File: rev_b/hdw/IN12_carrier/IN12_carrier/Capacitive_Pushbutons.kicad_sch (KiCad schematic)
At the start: 31 parts, among them J1001 Cap SNS

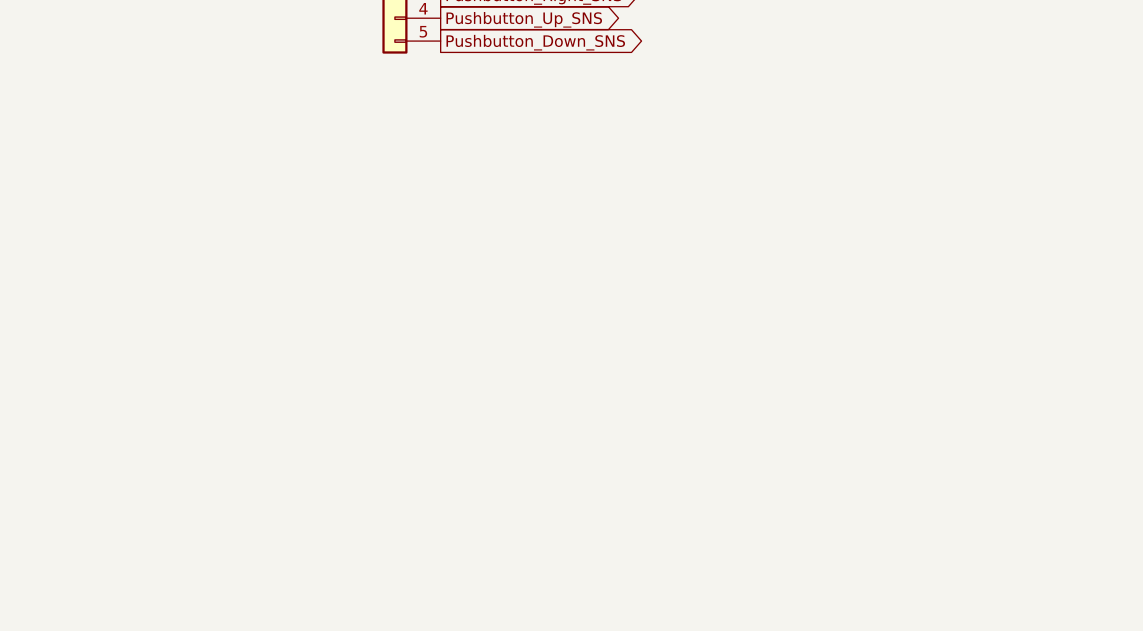
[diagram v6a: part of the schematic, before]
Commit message: added BOM for IN12 carrier, finished routing, some schematic tweaks, adjusted design rules for ERC
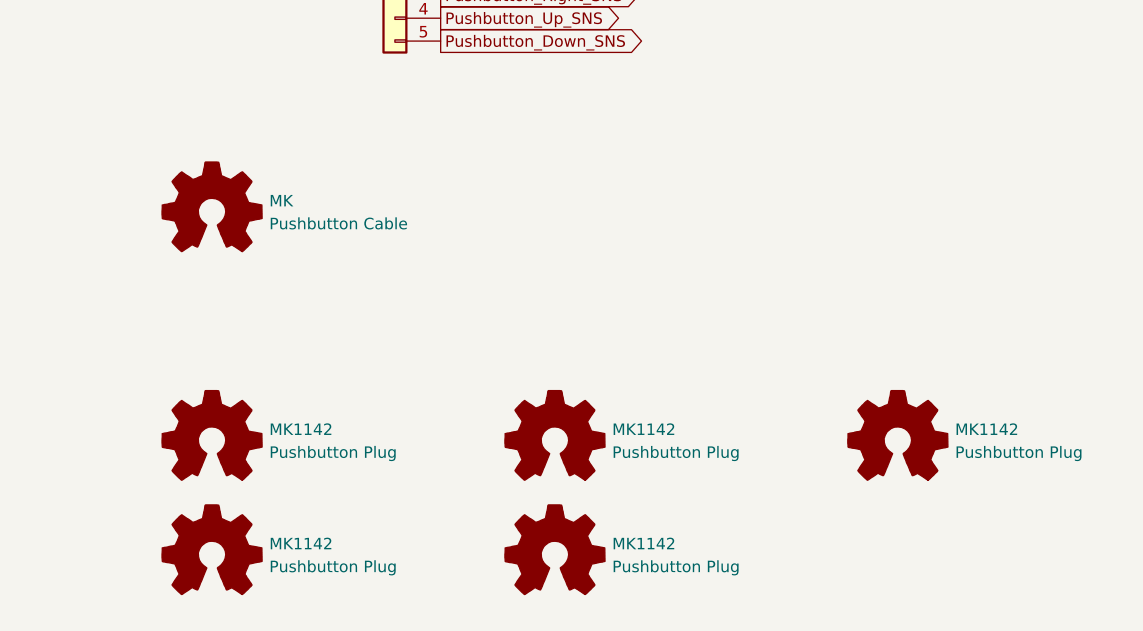
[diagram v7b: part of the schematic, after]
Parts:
- added MK: Pushbutton Cable, symbol Graphic:Logo_Open_Hardware_Small
- added MK1142 (x5): Pushbutton Plug, symbol Graphic:Logo_Open_Hardware_Small
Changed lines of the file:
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@@
+    )
+  )
+  (symbol (lib_id "Graphic:Logo_Open_Hardware_Small") (at 238.76 147.32 0) (unit 1)
+    (in_bom no) (on_board no) (dnp no) (fields_autoplaced)
+    (property "Reference" "MK1142" (at 245.11 146.05 0)
+      (effects (font (size 1.27 1.27)) (justify left))
+    )
+    (property "Value" "Pushbutton Plug" (at 245.11 148.59 0)
+      (effects (font (size 1.27 1.27)) (justify left))
+    )
+    (property "Footprint" "" (at 238.76 147.32 0)
+      (effects (font (size 1.27 1.27)) hide)
+    )
+    (property "Datasheet" "~" (at 238.76 147.32 0)
+      (effects (font (size 1.27 1.27)) hide)
+    )
+    (property "Digi-Key PN" "36-7600-ND" (at 238.76 147.32 0)
+      (effects (font (size 1.27 1.27)) hide)
+    )
+    (instances
+      (project "IN12_carrier"
+        (path "/c4d83a5b-e6ae-4326-9df5-0c4ac01f7d8c/3ccac04c-3fb1-4fbb-89c4-5dc2f5c153e1"
+          (reference "MK1142") (unit 1)
+        )
+        (path "/c4d83a5b-e6ae-4326-9df5-0c4ac01f7d8c/1c22c65e-aaf7-48af-ba9d-ccdda03c7a98"
+          (reference "MK1006") (unit 1)
+        )
+      )
     )
   )
@@
     )
   )
+  (symbol (lib_id "Graphic:Logo_Open_Hardware_Small") (at 162.56 160.02 0) (unit 1)
+    (in_bom no) (on_board no) (dnp no) (fields_autoplaced)
+    (property "Reference" "MK1142" (at 168.91 158.75 0)
+      (effects (font (size 1.27 1.27)) (justify left))
+    )
+    (property "Value" "Pushbutton Plug" (at 168.91 161.29 0)
+      (effects (font (size 1.27 1.27)) (justify left))
+    )
+    (property "Footprint" "" (at 162.56 160.02 0)
+      (effects (font (size 1.27 1.27)) hide)
+    )
+    (property "Datasheet" "~" (at 162.56 160.02 0)
+      (effects (font (size 1.27 1.27)) hide)
+    )
+    (property "Digi-Key PN" "36-7600-ND" (at 162.56 160.02 0)
+      (effects (font (size 1.27 1.27)) hide)
+    )
+    (instances
+      (project "IN12_carrier"
+        (path "/c4d83a5b-e6ae-4326-9df5-0c4ac01f7d8c/3ccac04c-3fb1-4fbb-89c4-5dc2f5c153e1"
+          (reference "MK1142") (unit 1)
+        )
+        (path "/c4d83a5b-e6ae-4326-9df5-0c4ac01f7d8c/1c22c65e-aaf7-48af-ba9d-ccdda03c7a98"
+          (reference "MK1003") (unit 1)
+        )
+      )
+    )
+  )
   (symbol (lib_id "power:GND") (at 104.14 158.75 0) (unit 1)
     (in_bom yes) (on_board yes) (dnp no)
@@
     )
   )
+  (symbol (lib_id "Graphic:Logo_Open_Hardware_Small") (at 162.56 147.32 0) (unit 1)
+    (in_bom no) (on_board no) (dnp no) (fields_autoplaced)
+    (property "Reference" "MK1142" (at 168.91 146.05 0)
+      (effects (font (size 1.27 1.27)) (justify left))
+    )
+    (property "Value" "Pushbutton Plug" (at 168.91 148.59 0)
+      (effects (font (size 1.27 1.27)) (justify left))
+    )
+    (property "Footprint" "" (at 162.56 147.32 0)
+      (effects (font (size 1.27 1.27)) hide)
+    )
+    (property "Datasheet" "~" (at 162.56 147.32 0)
+      (effects (font (size 1.27 1.27)) hide)
+    )
+    (property "Digi-Key PN" "36-7600-ND" (at 162.56 147.32 0)
+      (effects (font (size 1.27 1.27)) hide)
+    )
+    (instances
+      (project "IN12_carrier"
+        (path "/c4d83a5b-e6ae-4326-9df5-0c4ac01f7d8c/3ccac04c-3fb1-4fbb-89c4-5dc2f5c153e1"
+          (reference "MK1142") (unit 1)
+        )
+        (path "/c4d83a5b-e6ae-4326-9df5-0c4ac01f7d8c/1c22c65e-aaf7-48af-ba9d-ccdda03c7a98"
+          (reference "MK1002") (unit 1)
+        )
+      )
+    )
+  )
   (symbol (lib_id "Custom_Library:C_Custom") (at 198.12 43.18 0) (mirror y) (unit 1)
     (in_bom yes) (on_board yes) (dnp no)
@@
     )
   )
+  (symbol (lib_id "Graphic:Logo_Open_Hardware_Small") (at 200.66 147.32 0) (unit 1)
+    (in_bom no) (on_board no) (dnp no) (fields_autoplaced)
+    (property "Reference" "MK1142" (at 207.01 146.05 0)
+      (effects (font (size 1.27 1.27)) (justify left))
+    )
+    (property "Value" "Pushbutton Plug" (at 207.01 148.59 0)
+      (effects (font (size 1.27 1.27)) (justify left))
+    )
+    (property "Footprint" "" (at 200.66 147.32 0)
+      (effects (font (size 1.27 1.27)) hide)
+    )
+    (property "Datasheet" "~" (at 200.66 147.32 0)
+      (effects (font (size 1.27 1.27)) hide)
+    )
+    (property "Digi-Key PN" "36-7600-ND" (at 200.66 147.32 0)
+      (effects (font (size 1.27 1.27)) hide)
+    )
+    (instances
+      (project "IN12_carrier"
+        (path "/c4d83a5b-e6ae-4326-9df5-0c4ac01f7d8c/3ccac04c-3fb1-4fbb-89c4-5dc2f5c153e1"
+          (reference "MK1142") (unit 1)
+        )
+        (path "/c4d83a5b-e6ae-4326-9df5-0c4ac01f7d8c/1c22c65e-aaf7-48af-ba9d-ccdda03c7a98"
+          (reference "MK1004") (unit 1)
+        )
+      )
+    )
+  )
   (symbol (lib_id "power:GND") (at 76.2 151.13 0) (mirror y) (unit 1)
     (in_bom yes) (on_board yes) (dnp no)
@@
     )
   )
+  (symbol (lib_id "Graphic:Logo_Open_Hardware_Small") (at 200.66 160.02 0) (unit 1)
+    (in_bom no) (on_board no) (dnp no) (fields_autoplaced)
+    (property "Reference" "MK1142" (at 207.01 158.75 0)
+      (effects (font (size 1.27 1.27)) (justify left))
+    )
+    (property "Value" "Pushbutton Plug" (at 207.01 161.29 0)
+      (effects (font (size 1.27 1.27)) (justify left))
+    )
+    (property "Footprint" "" (at 200.66 160.02 0)
+      (effects (font (size 1.27 1.27)) hide)
+    )
+    (property "Datasheet" "~" (at 200.66 160.02 0)
+      (effects (font (size 1.27 1.27)) hide)
+    )
+    (property "Digi-Key PN" "36-7600-ND" (at 200.66 160.02 0)
+      (effects (font (size 1.27 1.27)) hide)
+    )
+    (instances
+      (project "IN12_carrier"
+        (path "/c4d83a5b-e6ae-4326-9df5-0c4ac01f7d8c/3ccac04c-3fb1-4fbb-89c4-5dc2f5c153e1"
+          (reference "MK1142") (unit 1)
+        )
+        (path "/c4d83a5b-e6ae-4326-9df5-0c4ac01f7d8c/1c22c65e-aaf7-48af-ba9d-ccdda03c7a98"
+          (reference "MK1005") (unit 1)
+        )
+      )
+    )
+  )
   (symbol (lib_id "power:+3.3V") (at 69.85 153.67 0) (unit 1)
     (in_bom yes) (on_board yes) (dnp no)
@@
         )
       )
+    )
+  )
+  (symbol (lib_id "Graphic:Logo_Open_Hardware_Small") (at 162.56 121.92 0) (unit 1)
+    (in_bom no) (on_board no) (dnp no) (fields_autoplaced)
+    (property "Reference" "MK" (at 168.91 120.65 0)
+      (effects (font (size 1.27 1.27)) (justify left))
+    )
+    (property "Value" "Pushbutton Cable" (at 168.91 123.19 0)
+      (effects (font (size 1.27 1.27)) (justify left))
+    )
+    (property "Footprint" "" (at 162.56 121.92 0)
+      (effects (font (size 1.27 1.27)) hide)
+    )
+    (property "Datasheet" "~" (at 162.56 121.92 0)
+      (effects (font (size 1.27 1.27)) hide)
+    )
+    (property "Digi-Key PN" "SAM8931-ND" (at 162.56 121.92 0)
+      (effects (font (size 1.27 1.27)) hide)
+    )
+    (instances
+      (project "IN12_carrier"
+        (path "/c4d83a5b-e6ae-4326-9df5-0c4ac01f7d8c/3ccac04c-3fb1-4fbb-89c4-5dc2f5c153e1"
+          (reference "MK") (unit 1)
+        )
+        (path "/c4d83a5b-e6ae-4326-9df5-0c4ac01f7d8c/1c22c65e-aaf7-48af-ba9d-ccdda03c7a98"
+          (reference "MK1001") (unit 1)
+        )
+      )

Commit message: assigned digikey pns to IN12 carrier board parts
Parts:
- C? (x10): Digi-Key PN (none) -> 1276-CL10B104KB8NNNLCT-ND
- C? (x5): Digi-Key PN (none) -> 1276-1009-1-ND
- R? (x5): Digi-Key PN (none) -> 541-CRCW0603499RFKEBCT-ND
- R? (x5): Digi-Key PN (none) -> 541-10.0KHCT-ND
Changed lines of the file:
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@@
       (effects (font (size 1.27 1.27)) hide)
     )
-    (property "Digi-Key PN" "" (at 36.83 110.49 0)
+    (property "Digi-Key PN" "541-CRCW0603499RFKEBCT-ND" (at 36.83 110.49 0)
       (effects (font (size 1.524 1.524)) hide)
     )
@@
       (effects (font (size 1.27 1.27)) hide)
     )
-    (property "Digi-Key PN" "" (at 59.055 30.48 0)
+    (property "Digi-Key PN" "1276-CL10B104KB8NNNLCT-ND" (at 59.055 30.48 0)
       (effects (font (size 1.524 1.524)) hide)
     )
@@
       (effects (font (size 1.27 1.27)) hide)
     )
-    (property "Digi-Key PN" "" (at 36.83 72.39 0)
+    (property "Digi-Key PN" "541-CRCW0603499RFKEBCT-ND" (at 36.83 72.39 0)
       (effects (font (size 1.524 1.524)) hide)
     )
@@
       (effects (font (size 1.27 1.27)) (justify left) hide)
     )
-    (property "Digi-Key PN" "" (at 99.06 144.78 0)
+    (property "Digi-Key PN" "541-10.0KHCT-ND" (at 99.06 144.78 0)
       (effects (font (size 1.524 1.524)) hide)
     )
@@
       (effects (font (size 1.27 1.27)) hide)
     )
-    (property "Digi-Key PN" "" (at 36.83 34.29 0)
+    (property "Digi-Key PN" "541-CRCW0603499RFKEBCT-ND" (at 36.83 34.29 0)
       (effects (font (size 1.524 1.524)) hide)
     )
@@
       (effects (font (size 1.27 1.27)) (justify left) hide)
     )
-    (property "Digi-Key PN" "" (at 99.06 30.48 0)
+    (property "Digi-Key PN" "541-10.0KHCT-ND" (at 99.06 30.48 0)
       (effects (font (size 1.524 1.524)) hide)
     )
@@
       (effects (font (size 1.27 1.27)) hide)
     )
-    (property "Digi-Key PN" "" (at 93.345 27.94 0)
+    (property "Digi-Key PN" "1276-CL10B104KB8NNNLCT-ND" (at 93.345 27.94 0)
       (effects (font (size 1.524 1.524)) hide)
     )
@@
       (effects (font (size 1.27 1.27)) hide)
     )
-    (property "Digi-Key PN" "" (at 59.055 68.58 0)
+    (property "Digi-Key PN" "1276-CL10B104KB8NNNLCT-ND" (at 59.055 68.58 0)
       (effects (font (size 1.524 1.524)) hide)
     )
@@
       (effects (font (size 1.27 1.27)) hide)
     )
-    (property "Digi-Key PN" "" (at 221.615 27.94 0)
+    (property "Digi-Key PN" "1276-CL10B104KB8NNNLCT-ND" (at 221.615 27.94 0)
       (effects (font (size 1.524 1.524)) hide)
     )
@@
       (effects (font (size 1.27 1.27)) hide)
     )
-    (property "Digi-Key PN" "" (at 36.83 148.59 0)
+    (property "Digi-Key PN" "541-CRCW0603499RFKEBCT-ND" (at 36.83 148.59 0)
       (effects (font (size 1.524 1.524)) hide)
     )
@@
       (effects (font (size 1.27 1.27)) (justify left) hide)
     )
-    (property "Digi-Key PN" "" (at 99.06 106.68 0)
+    (property "Digi-Key PN" "541-10.0KHCT-ND" (at 99.06 106.68 0)
       (effects (font (size 1.524 1.524)) hide)
     )
@@
       (effects (font (size 1.27 1.27)) (justify left) hide)
     )
-    (property "Digi-Key PN" "" (at 227.33 30.48 0)
+    (property "Digi-Key PN" "541-10.0KHCT-ND" (at 227.33 30.48 0)
       (effects (font (size 1.524 1.524)) hide)
     )
@@
       (effects (font (size 1.27 1.27)) hide)
     )
-    (property "Digi-Key PN" "" (at 187.325 30.48 0)
+    (property "Digi-Key PN" "1276-CL10B104KB8NNNLCT-ND" (at 187.325 30.48 0)
       (effects (font (size 1.524 1.524)) hide)
     )
@@
       (effects (font (size 1.27 1.27)) hide)
     )
-    (property "Digi-Key PN" "" (at 59.055 106.68 0)
+    (property "Digi-Key PN" "1276-CL10B104KB8NNNLCT-ND" (at 59.055 106.68 0)
       (effects (font (size 1.524 1.524)) hide)
     )
@@
       (effects (font (size 1.27 1.27)) hide)
     )
-    (property "Digi-Key PN" "" (at 93.345 66.04 0)
+    (property "Digi-Key PN" "1276-CL10B104KB8NNNLCT-ND" (at 93.345 66.04 0)
       (effects (font (size 1.524 1.524)) hide)
     )
@@
       (effects (font (size 1.27 1.27)) hide)
     )
-    (property "Digi-Key PN" "" (at 3.302 229.616 0)
+    (property "Digi-Key PN" "1276-1009-1-ND" (at 3.302 229.616 0)
       (effects (font (size 1.27 1.27)) hide)
     )
@@
       (effects (font (size 1.27 1.27)) hide)
     )
-    (property "Digi-Key PN" "" (at 93.345 104.14 0)
+    (property "Digi-Key PN" "1276-CL10B104KB8NNNLCT-ND" (at 93.345 104.14 0)
       (effects (font (size 1.524 1.524)) hide)
     )
@@
       (effects (font (size 1.27 1.27)) hide)
     )
-    (property "Digi-Key PN" "" (at 131.572 153.416 0)
+    (property "Digi-Key PN" "1276-1009-1-ND" (at 131.572 153.416 0)
       (effects (font (size 1.27 1.27)) hide)
     )
@@
       (effects (font (size 1.27 1.27)) hide)
     )
-    (property "Digi-Key PN" "" (at 3.302 191.516 0)
+    (property "Digi-Key PN" "1276-1009-1-ND" (at 3.302 191.516 0)
       (effects (font (size 1.27 1.27)) hide)
     )
@@
       (effects (font (size 1.27 1.27)) hide)
     )
-    (property "Digi-Key PN" "" (at 59.055 144.78 0)
+    (property "Digi-Key PN" "1276-CL10B104KB8NNNLCT-ND" (at 59.055 144.78 0)
       (effects (font (size 1.524 1.524)) hide)
     )
@@
       (effects (font (size 1.27 1.27)) (justify left) hide)
     )
-    (property "Digi-Key PN" "" (at 99.06 68.58 0)
+    (property "Digi-Key PN" "541-10.0KHCT-ND" (at 99.06 68.58 0)
       (effects (font (size 1.524 1.524)) hide)
     )
@@
       (effects (font (size 1.27 1.27)) hide)
     )
-    (property "Digi-Key PN" "" (at 3.302 153.416 0)
+    (property "Digi-Key PN" "1276-1009-1-ND" (at 3.302 153.416 0)
       (effects (font (size 1.27 1.27)) hide)
     )
@@
       (effects (font (size 1.27 1.27)) hide)
     )
-    (property "Digi-Key PN" "" (at 3.302 267.716 0)
+    (property "Digi-Key PN" "1276-1009-1-ND" (at 3.302 267.716 0)
       (effects (font (size 1.27 1.27)) hide)
     )
@@
       (effects (font (size 1.27 1.27)) hide)
     )
-    (property "Digi-Key PN" "" (at 93.345 142.24 0)
+    (property "Digi-Key PN" "1276-CL10B104KB8NNNLCT-ND" (at 93.345 142.24 0)
       (effects (font (size 1.524 1.524)) hide)
     )
@@
       (effects (font (size 1.27 1.27)) hide)
     )
-    (property "Digi-Key PN" "" (at 165.1 34.29 0)
+    (property "Digi-Key PN" "541-CRCW0603499RFKEBCT-ND" (at 165.1 34.29 0)
       (effects (font (size 1.524 1.524)) hide)
     )
